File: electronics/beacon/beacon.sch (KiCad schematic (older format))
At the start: 15 parts, among them J1 CONN_02X02, J2 CONN_02X02, J3 Rails, Q1 Q_NMOS_GSD, U1 ATTINY45-20XUR, U2 TPS70928DBV

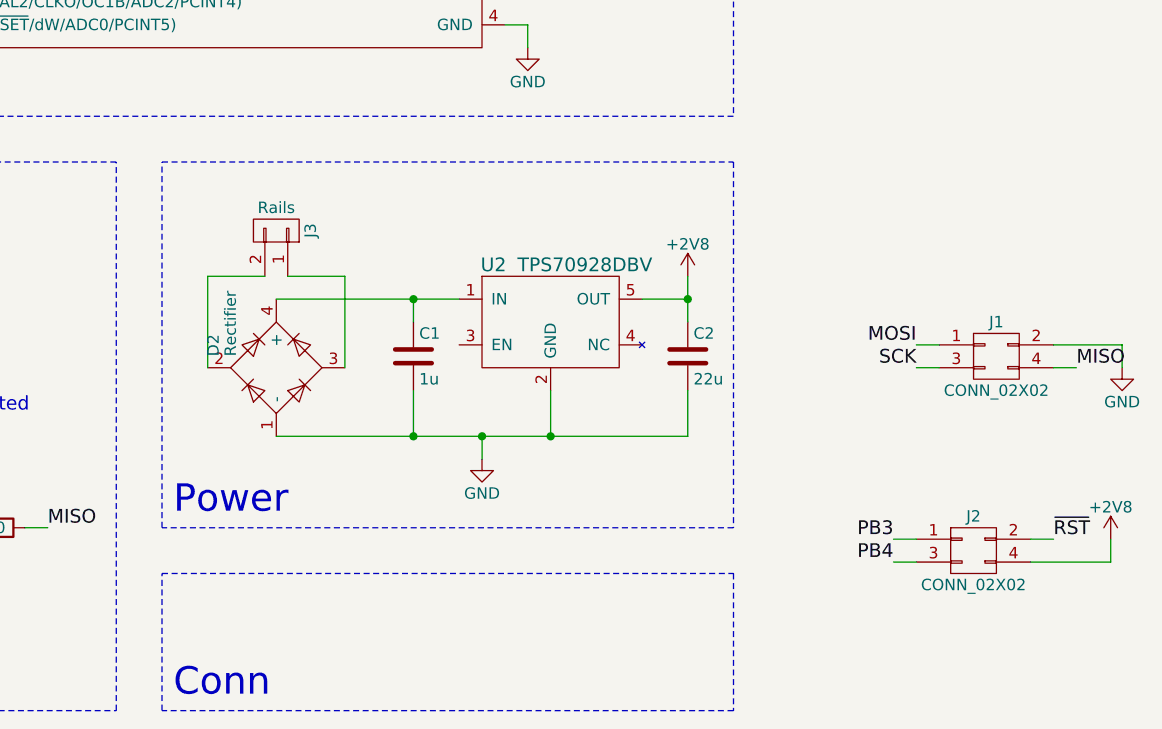
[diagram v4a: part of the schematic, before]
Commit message: electronics: beacon: Final beacon board Rev 1.0
- increase board size to fit all components
- add rail and connector footprints to library
- improve track mechanical model
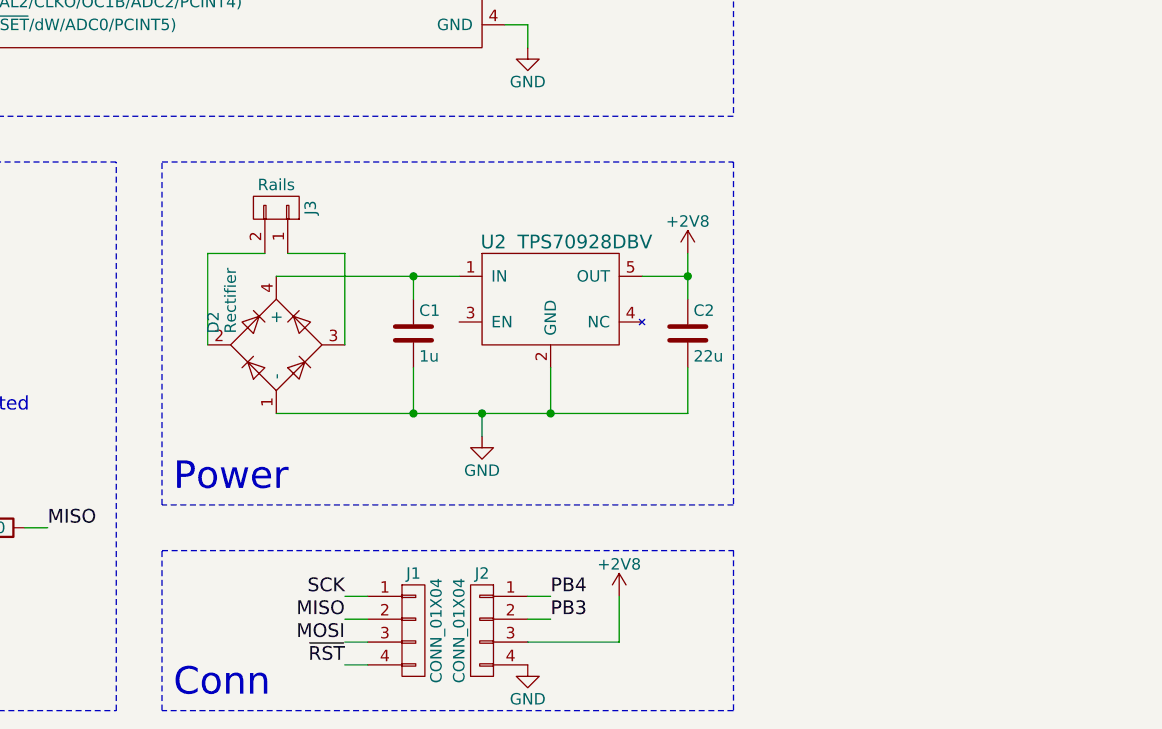
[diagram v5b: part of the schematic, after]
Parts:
- removed J1, J2: CONN_02X02, bcan:Edge_Connector_2x02_Pitch2.54mm_SMD, symbol CONN_02X02
- added J1, J2: CONN_01X04, bcan:Edge_Connector_1x04_Pitch2.54mm_SMD, symbol CONN_01X04
- J3: footprint bcan:HO_Rail_2_Length3.5mm_Width3mm -> bcan:HO_Rail_2_Length2.4mm_Width4mm
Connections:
- net +2V8: now also J2.3 (P3)
- net GND: now also J2.4 (P4)
- net MISO: now also J1.2 (P2)
- net MOSI: now also J1.3 (P3)
- net PB3: now also J2.2 (P2)
- net PB4: now also J2.1 (P1)
- net SCK: now also J1.1 (P1)
- net ~RST: now also J1.4 (P4)
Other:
- moved on the sheet: C1, C2, D2, J3, U2
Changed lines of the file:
@@
 L D_Bridge_-AA+ D2
 U 1 1 58916D19
-P 6200 4700
-F 0 "D2" H 6250 4975 50  0000 L CNN
-F 1 "Rectifier" H 6250 4900 50  0000 L CNN
-F 2 "TO_SOT_Packages_SMD:SOT-143" H 6200 4700 50  0001 C CNN
-F 3 "" H 6200 4700 50  0000 C CNN
-	1    6200 4700
+P 6200 4600
+F 0 "D2" H 6250 4875 50  0000 L CNN
+F 1 "Rectifier" H 6250 4800 50  0000 L CNN
+F 2 "TO_SOT_Packages_SMD:SOT-143" H 6200 4600 50  0001 C CNN
+F 3 "" H 6200 4600 50  0000 C CNN
+	1    6200 4600
 	0    -1   -1   0
 $EndComp
@@
 L GND #PWR01
 U 1 1 58919FC5
-P 7100 5100
-F 0 "#PWR01" H 7100 4850 50  0001 C CNN
-F 1 "GND" H 7100 4950 50  0000 C CNN
-F 2 "" H 7100 5100 50  0000 C CNN
-F 3 "" H 7100 5100 50  0000 C CNN
-	1    7100 5100
+P 7100 5000
+F 0 "#PWR01" H 7100 4750 50  0001 C CNN
+F 1 "GND" H 7100 4850 50  0000 C CNN
+F 2 "" H 7100 5000 50  0000 C CNN
+F 3 "" H 7100 5000 50  0000 C CNN
+	1    7100 5000
 	1    0    0    -1
 $EndComp
@@
 L C C1
 U 1 1 5893B026
-P 6800 4650
-F 0 "C1" H 6825 4750 50  0000 L CNN
-F 1 "1u" H 6825 4550 50  0000 L CNN
-F 2 "Capacitors_SMD:C_0603" H 6838 4500 50  0001 C CNN
-F 3 "" H 6800 4650 50  0000 C CNN
-	1    6800 4650
+P 6800 4550
+F 0 "C1" H 6825 4650 50  0000 L CNN
+F 1 "1u" H 6825 4450 50  0000 L CNN
+F 2 "Capacitors_SMD:C_0603" H 6838 4400 50  0001 C CNN
+F 3 "" H 6800 4550 50  0000 C CNN
+	1    6800 4550
 	1    0    0    -1
 $EndComp
@@
 L +2V8 #PWR04
 U 1 1 58AA1702
-P 8000 4300
-F 0 "#PWR04" H 8000 4150 50  0001 C CNN
-F 1 "+2V8" H 8000 4440 50  0000 C CNN
-F 2 "" H 8000 4300 50  0001 C CNN
-F 3 "" H 8000 4300 50  0001 C CNN
-	1    8000 4300
+P 8000 4200
+F 0 "#PWR04" H 8000 4050 50  0001 C CNN
+F 1 "+2V8" H 8000 4340 50  0000 C CNN
+F 2 "" H 8000 4200 50  0001 C CNN
+F 3 "" H 8000 4200 50  0001 C CNN
+	1    8000 4200
 	1    0    0    -1
 $EndComp
@@
 L TPS70928DBV U2
 U 1 1 58AB0B0D
-P 7400 4500
-F 0 "U2" H 7150 4750 60  0000 C CNN
-F 1 "TPS70928DBV" H 7550 4750 60  0000 C CNN
-F 2 "TO_SOT_Packages_SMD:SOT-23-5" H 7400 4500 60  0001 C CNN
-F 3 "" H 7400 4500 60  0001 C CNN
-	1    7400 4500
+P 7400 4400
+F 0 "U2" H 7150 4650 60  0000 C CNN
+F 1 "TPS70928DBV" H 7550 4650 60  0000 C CNN
+F 2 "TO_SOT_Packages_SMD:SOT-23-5" H 7400 4400 60  0001 C CNN
+F 3 "" H 7400 4400 60  0001 C CNN
+	1    7400 4400
 	1    0    0    -1
 $EndComp
@@
 L C C2
 U 1 1 58AB22F8
-P 8000 4650
-F 0 "C2" H 8025 4750 50  0000 L CNN
-F 1 "22u" H 8025 4550 50  0000 L CNN
-F 2 "Capacitors_SMD:C_0603" H 8038 4500 50  0001 C CNN
-F 3 "" H 8000 4650 50  0001 C CNN
-	1    8000 4650
+P 8000 4550
+F 0 "C2" H 8025 4650 50  0000 L CNN
+F 1 "22u" H 8025 4450 50  0000 L CNN
+F 2 "Capacitors_SMD:C_0603" H 8038 4400 50  0001 C CNN
+F 3 "" H 8000 4550 50  0001 C CNN
+	1    8000 4550
 	1    0    0    -1
 $EndComp
@@
 Text Notes 3650 3550 0    120  ~ 0
 Control
-Text Notes 5750 5350 0    120  ~ 0
+Text Notes 5750 5250 0    120  ~ 0
 Power
 Text Notes 3650 6150 0    120  ~ 0
@@
 L CONN_01X02 J3
 U 1 1 58C5B8EB
-P 6200 4100
-F 0 "J3" H 6200 4250 50  0000 C CNN
-F 1 "Rails" V 6300 4100 50  0000 C CNN
-F 2 "bcan:HO_Rail_2_Length3.5mm_Width3mm" H 6200 4100 50  0001 C CNN
-F 3 "" H 6200 4100 50  0001 C CNN
-	1    6200 4100
+P 6200 4000
+F 0 "J3" H 6200 4150 50  0000 C CNN
+F 1 "Rails" V 6300 4000 50  0000 C CNN
+F 2 "bcan:HO_Rail_2_Length2.4mm_Width4mm" H 6200 4000 50  0001 C CNN
+F 3 "" H 6200 4000 50  0001 C CNN
+	1    6200 4000
 	0    1    -1   0
 $EndComp
@@
 Conn
 $Comp
-L CONN_02X02 J1
-U 1 1 58C61A56
-P 9350 4650
-F 0 "J1" H 9350 4800 50  0000 C CNN
-F 1 "CONN_02X02" H 9350 4500 50  0000 C CNN
-F 2 "bcan:Edge_Connector_2x02_Pitch2.54mm_SMD" H 9350 3450 50  0001 C CNN
-F 3 "" H 9350 3450 50  0001 C CNN
-	1    9350 4650
-	1    0    0    -1
-$EndComp
-$Comp
-L CONN_02X02 J2
-U 1 1 58C61B0B
-P 9250 5500
-F 0 "J2" H 9250 5650 50  0000 C CNN
-F 1 "CONN_02X02" H 9250 5350 50  0000 C CNN
-F 2 "bcan:Edge_Connector_2x02_Pitch2.54mm_SMD" H 9250 4300 50  0001 C CNN
-F 3 "" H 9250 4300 50  0001 C CNN
-	1    9250 5500
-	1    0    0    -1
-$EndComp
-Text Label 9000 4600 2    60   ~ 0
-MOSI
-Text Label 9000 4700 2    60   ~ 0
-SCK
-$Comp
 L +2V8 #PWR08
 U 1 1 58C62508
-P 9850 5450
-F 0 "#PWR08" H 9850 5300 50  0001 C CNN
-F 1 "+2V8" H 9850 5590 50  0000 C CNN
-F 2 "" H 9850 5450 50  0001 C CNN
-F 3 "" H 9850 5450 50  0001 C CNN
-	1    9850 5450
-	1    0    0    -1
-$EndComp
-Wire Wire Line
-	9100 4700 9000 4700
-Wire Wire Line
-	9100 4600 9000 4600
-Wire Wire Line
-	9000 5550 8900 5550
-Wire Wire Line
-	9000 5450 8900 5450
-Wire Wire Line
-	9500 5450 9600 5450
-Wire Notes Line
-	5700 6200 5700 5600
+P 7700 5700
+F 0 "#PWR08" H 7700 5550 50  0001 C CNN
+F 1 "+2V8" H 7700 5840 50  0000 C CNN
+F 2 "" H 7700 5700 50  0001 C CNN
+F 3 "" H 7700 5700 50  0001 C CNN
+	1    7700 5700
+	1    0    0    -1
+$EndComp
+$Comp
+L GND #PWR09
+U 1 1 58C62B36
+P 7300 6000
+F 0 "#PWR09" H 7300 5750 50  0001 C CNN
+F 1 "GND" H 7300 5850 50  0000 C CNN
+F 2 "" H 7300 6000 50  0001 C CNN
+F 3 "" H 7300 6000 50  0001 C CNN
+	1    7300 6000
+	1    0    0    -1
+$EndComp
+$Comp
+L CONN_01X04 J1
+U 1 1 58CB22C8
+P 6800 5850
+F 0 "J1" H 6800 6100 50  0000 C CNN
+F 1 "CONN_01X04" V 6900 5850 50  0000 C CNN
+F 2 "bcan:Edge_Connector_1x04_Pitch2.54mm_SMD" H 6800 5850 50  0001 C CNN
+F 3 "" H 6800 5850 50  0001 C CNN
+	1    6800 5850
+	1    0    0    -1
+$EndComp
+$Comp
+L CONN_01X04 J2
+U 1 1 58CB236F
+P 7100 5850
+F 0 "J2" H 7100 6100 50  0000 C CNN
+F 1 "CONN_01X04" V 7200 5850 50  0000 C CNN
+F 2 "bcan:Edge_Connector_1x04_Pitch2.54mm_SMD" H 7100 5850 50  0001 C CNN
+F 3 "" H 7100 5850 50  0001 C CNN
+	1    7100 5850
+	-1   0    0    -1
+$EndComp
+Wire Notes Line
+	5700 6200 5700 5500
 Wire Notes Line
 	8200 6200 5700 6200
 Wire Notes Line
-	8200 5600 8200 6200
-Wire Notes Line
-	5700 5600 8200 5600
-Wire Wire Line
-	7800 4400 8000 4400
+	8200 5500 8200 6200
+Wire Notes Line
+	5700 5500 8200 5500
+Wire Wire Line
+	7800 4300 8000 4300
 Wire Notes Line
 	4950 4900 4500 4900
@@
 Wire Wire Line
 	7200 2700 7300 2700
-Connection ~ 8000 4400
-Wire Wire Line
-	8000 4300 8000 4500
+Connection ~ 8000 4300
+Wire Wire Line
+	8000 4200 8000 4400
 Connection ~ 4700 5400
 Connection ~ 4500 5800
@@
 	4200 5000 4200 5100
 Wire Wire Line
-	8000 5000 8000 4800
-Connection ~ 6800 5000
-Wire Wire Line
-	6800 5000 6800 4800
+	8000 4900 8000 4700
+Connection ~ 6800 4900
+Wire Wire Line
+	6800 4900 6800 4700
 Wire Wire Line
 	7200 3200 7300 3200
@@
 	7300 3200 7300 3300
 Wire Wire Line
-	7100 5000 7100 5100
-Connection ~ 7100 5000
-Wire Wire Line
-	7400 5000 7400 4800
-Connection ~ 7400 5000
-Wire Wire Line
-	6200 5000 8000 5000
+	7100 4900 7100 5000
+Connection ~ 7100 4900
+Wire Wire Line
+	7400 4900 7400 4700
+Connection ~ 7400 4900
+Wire Wire Line
+	6200 4900 8000 4900
 Wire Wire Line
 	5100 5400 5200 5400
@@
 	8200 2300 8200 3600
 Wire Notes Line
-	5700 5400 5700 3800
+	5700 5300 5700 3800
 Wire Notes Line
 	5700 3800 8200 3800
 Wire Notes Line
-	8200 3800 8200 5400
-Wire Notes Line
-	8200 5400 5700 5400
+	8200 3800 8200 5300
+Wire Notes Line
+	8200 5300 5700 5300
 Wire Notes Line
 	5500 6200 5500 3800
@@
 	4600 3000 4500 3000
 Wire Wire Line
-	6200 4400 7000 4400
-Wire Wire Line
-	6800 4500 6800 4400
-Connection ~ 6800 4400
-Wire Wire Line
-	6150 4300 5900 4300
-Wire Wire Line
-	5900 4300 5900 4700
-Wire Wire Line
-	6250 4300 6500 4300
-Wire Wire Line
-	6500 4300 6500 4700
-Text Label 9600 5450 0    60   ~ 0
+	6200 4300 7000 4300
+Wire Wire Line
+	6800 4400 6800 4300
+Connection ~ 6800 4300
+Wire Wire Line
+	6150 4200 5900 4200
+Wire Wire Line
+	5900 4200 5900 4600
+Wire Wire Line
+	6250 4200 6500 4200
+Wire Wire Line
+	6500 4200 6500 4600
+Wire Wire Line
+	7300 5900 7700 5900
+Wire Wire Line
+	7700 5900 7700 5700
+Wire Wire Line
+	7300 5800 7400 5800
+Wire Wire Line
+	7300 5700 7400 5700
+Text Label 7400 5800 0    60   ~ 0
+PB3
+Text Label 7400 5700 0    60   ~ 0
+PB4
+Wire Wire Line
+	6600 6000 6500 6000
+Wire Wire Line
+	6600 5900 6500 5900
+Wire Wire Line
+	6600 5800 6500 5800
+Wire Wire Line
+	6600 5700 6500 5700
+Text Label 6500 6000 2    60   ~ 0
 ~RST
-Text Label 8900 5450 2    60   ~ 0
-PB3
-Text Label 8900 5550 2    60   ~ 0
-PB4
-Wire Wire Line
-	9500 5550 9850 5550
-Wire Wire Line
-	9850 5550 9850 5450
-$Comp
-L GND #PWR09
-U 1 1 58C62B36
-P 9900 4700
-F 0 "#PWR09" H 9900 4450 50  0001 C CNN
-F 1 "GND" H 9900 4550 50  0000 C CNN
-F 2 "" H 9900 4700 50  0001 C CNN
-F 3 "" H 9900 4700 50  0001 C CNN
-	1    9900 4700
-	1    0    0    -1
-$EndComp
-Wire Wire Line
-	9600 4600 9900 4600
-Wire Wire Line
-	9900 4600 9900 4700
-Wire Wire Line
-	9600 4700 9700 4700
-Text Label 9700 4700 0    60   ~ 0
+Text Label 6500 5900 2    60   ~ 0
+MOSI
+Text Label 6500 5800 2    60   ~ 0
 MISO
+Text Label 6500 5700 2    60   ~ 0
+SCK
 $EndSCHEMATC

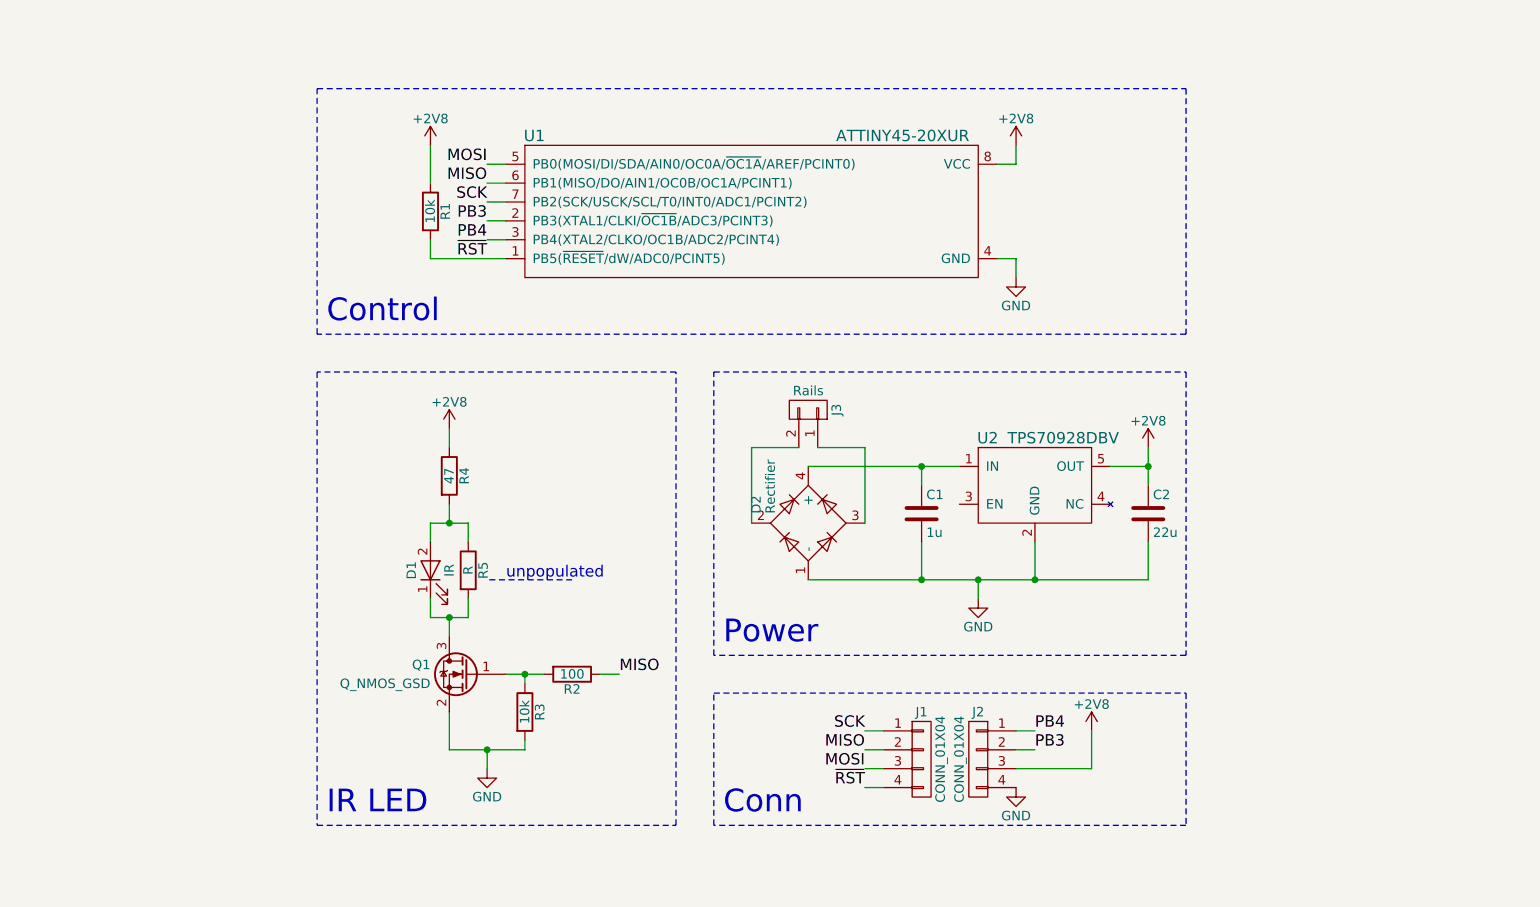
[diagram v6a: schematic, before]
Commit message: electronics: beacon: Improve schematic labeling & readability
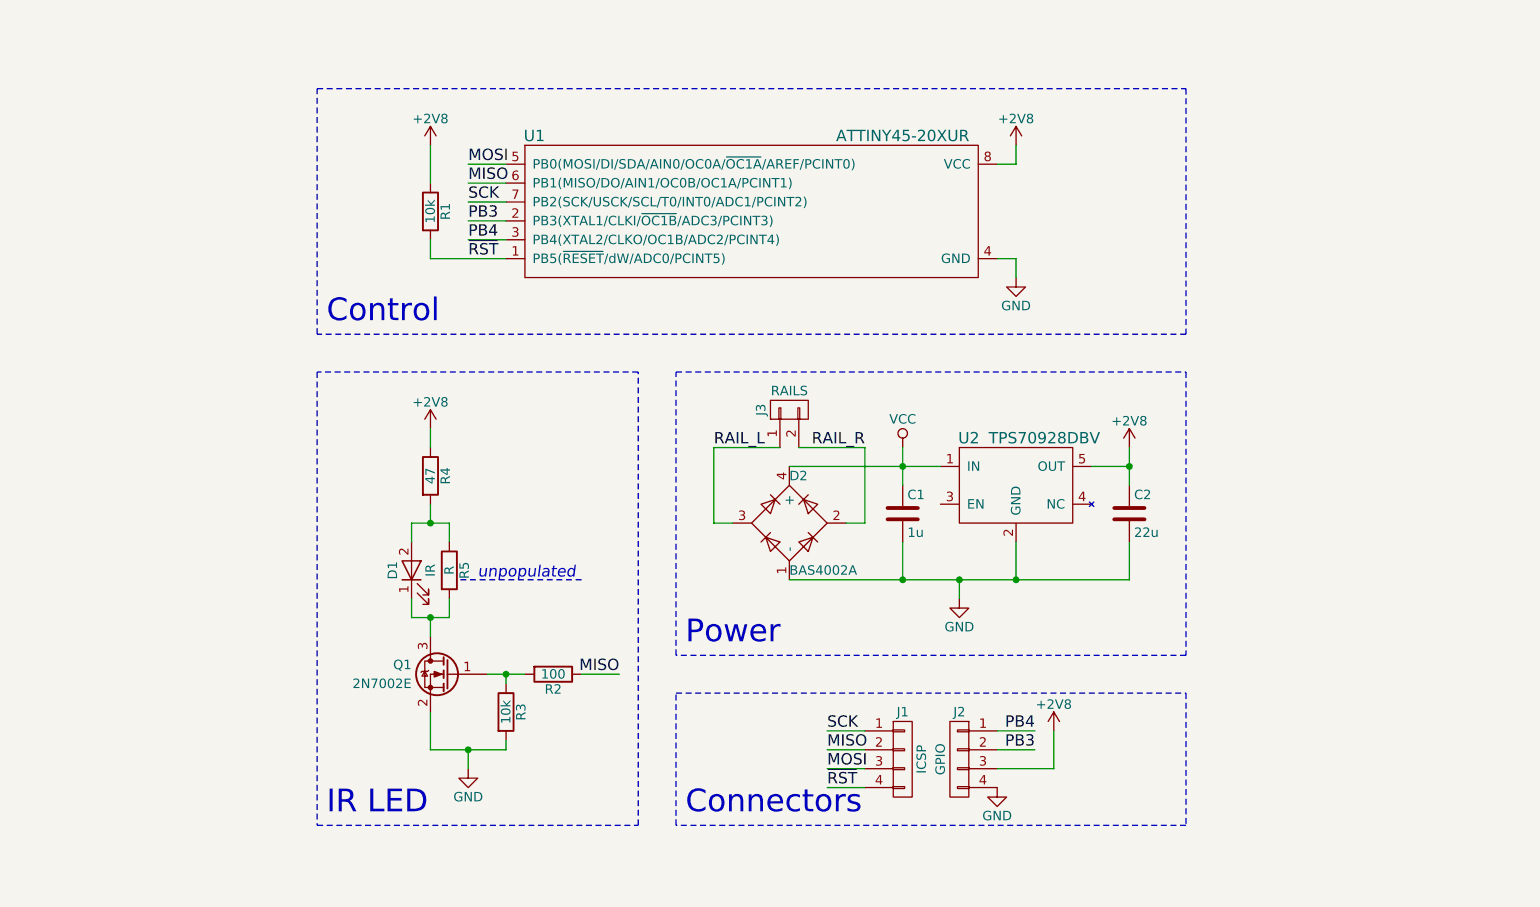
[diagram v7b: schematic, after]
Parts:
- D2: value Rectifier -> BAS4002A
- J1: value CONN_01X04 -> ICSP
- J2: value CONN_01X04 -> GPIO
- J3: value Rails -> RAILS
- Q1: value Q_NMOS_GSD -> 2N7002E
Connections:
- net RAIL_R: now reaches D2.2, J3.2 (P2)
- net RAIL_L: now reaches D2.3, J3.1 (P1)
- net VCC: now reaches C1.1, D2.4 (+), U2.1 (IN)
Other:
- note added: "Connectors"
- note removed: "Conn"
- moved on the sheet: C1, C2, D1, D2, J1, J2, J3, Q1, R2, R3, R4, R5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
